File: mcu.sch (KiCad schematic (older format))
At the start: 44 parts, among them J10 DX07S016JA1R1500, J11 I2Sext_SD, J12 I2S_SD, J13 SDOUT, J14 ~CSB, J15 I2S2_MCK, J16 WCLK, J17 BCLK, J18 SCLK, J7 PD0-7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

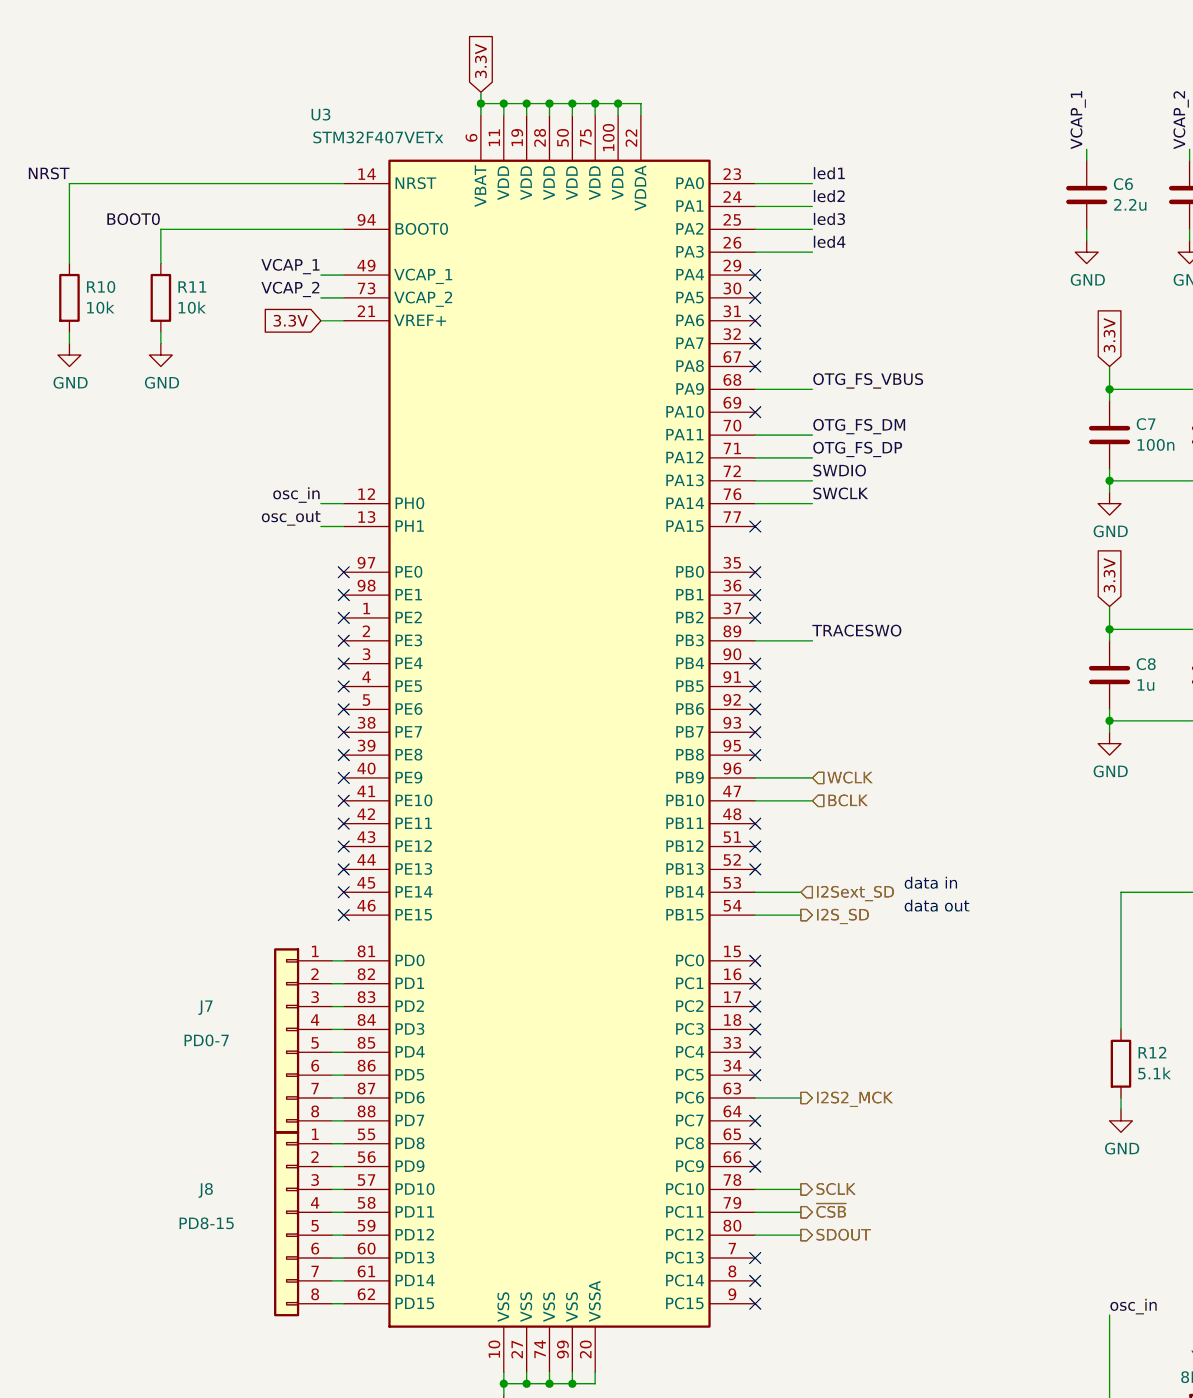
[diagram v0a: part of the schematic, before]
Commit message: Update pins for actual ADC ins
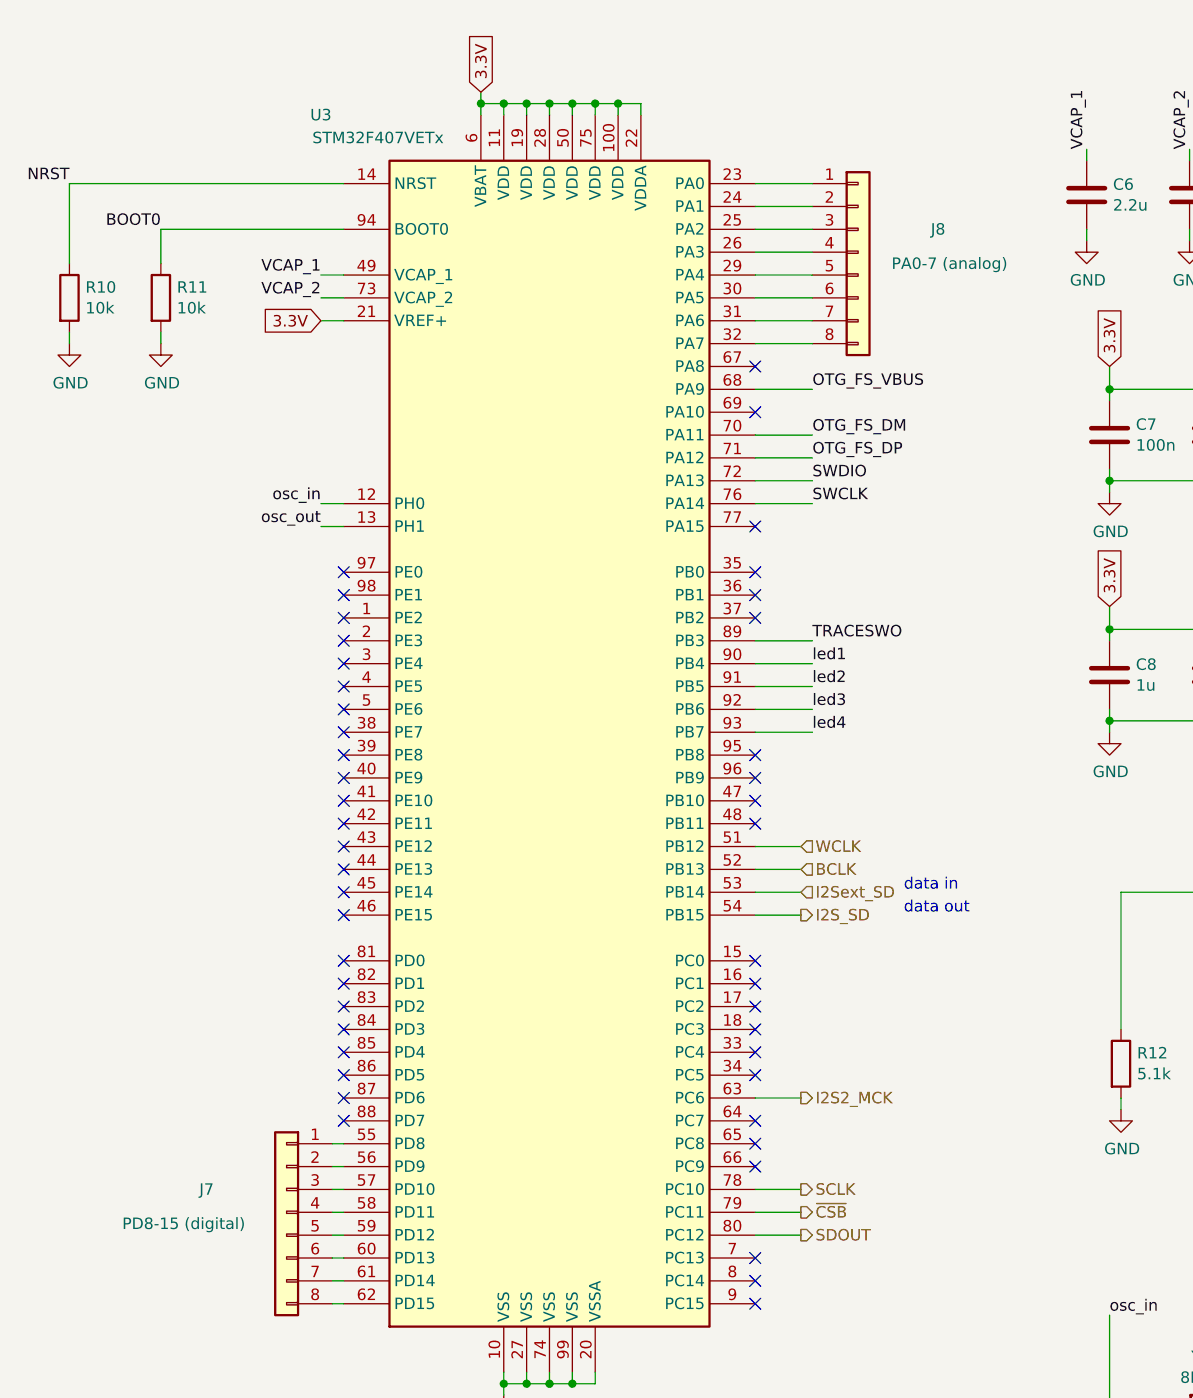
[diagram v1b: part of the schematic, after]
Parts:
- removed J7: PD0-7, Connector_PinHeader_2.54mm:PinHeader_1x08_P2.54mm_Vertical, symbol Connector_Generic:Conn_01x08
- added J8: PA0-7 (analog), Connector_PinHeader_2.54mm:PinHeader_1x08_P2.54mm_Vertical, symbol Connector_Generic:Conn_01x08
- J7: renamed from J8; value PD8-15 -> PD8-15 (digital)
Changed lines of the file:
@@
 	1950 5400 2000 5400
 $Comp
-L Connector_Generic:Conn_01x08 J8
+L Connector_Generic:Conn_01x08 J7
 U 1 1 605BF3D9
 P 1750 5700
-F 0 "J8" H 2100 5800 50  0000 C CNN
-F 1 "PD8-15" H 2100 5650 50  0000 C CNN
+F 0 "J7" H 2100 5800 50  0000 C CNN
+F 1 "PD8-15 (digital)" H 2200 5650 50  0000 C CNN
 F 2 "Connector_PinHeader_2.54mm:PinHeader_1x08_P2.54mm_Vertical" H 1750 5700 50  0001 C CNN
 F 3 "~" H 1750 5700 50  0001 C CNN
 	1    1750 5700
-	-1   0    0    -1
-$EndComp
-$Comp
-L Connector_Generic:Conn_01x08 J7
-U 1 1 605777EA
-P 1750 4900
-F 0 "J7" H 2100 5000 50  0000 C CNN
-F 1 "PD0-7" H 2100 4850 50  0000 C CNN
-F 2 "Connector_PinHeader_2.54mm:PinHeader_1x08_P2.54mm_Vertical" H 1750 4900 50  0001 C CNN
-F 3 "~" H 1750 4900 50  0001 C CNN
-	1    1750 4900
 	-1   0    0    -1
 $EndComp
@@
 Wire Wire Line
 	4050 1200 3800 1200
-Text Label 4050 1500 0    50   ~ 0
+Text Label 4050 3600 0    50   ~ 0
 led4
-Text Label 4050 1400 0    50   ~ 0
+Text Label 4050 3500 0    50   ~ 0
 led3
-Text Label 4050 1300 0    50   ~ 0
+Text Label 4050 3400 0    50   ~ 0
 led2
-Text Label 4050 1200 0    50   ~ 0
+Text Label 4050 3300 0    50   ~ 0
 led1
-Wire Wire Line
-	1950 5300 2000 5300
-Wire Wire Line
-	1950 5200 2000 5200
-Wire Wire Line
-	1950 5100 2000 5100
-Wire Wire Line
-	1950 5000 2000 5000
-Wire Wire Line
-	1950 4900 2000 4900
-Wire Wire Line
-	1950 4800 2000 4800
-Wire Wire Line
-	1950 4700 2000 4700
-Wire Wire Line
-	1950 4600 2000 4600
 Text Label 1900 2700 2    50   ~ 0
 osc_out
@@
 SWDIO
 Wire Wire Line
-	4050 3900 3800 3900
-Wire Wire Line
-	4050 3800 3800 3800
+	4000 4200 3800 4200
+Wire Wire Line
+	4000 4100 3800 4100
 Text Notes 4450 4400 0    50   ~ 0
 data out
@@
 Text HLabel 4000 4400 2    50   Output ~ 0
 I2S_SD
-Text HLabel 4050 3800 2    50   Input ~ 0
+Text HLabel 4000 4100 2    50   Input ~ 0
 WCLK
-Text HLabel 4050 3900 2    50   Input ~ 0
+Text HLabel 4000 4200 2    50   Input ~ 0
 BCLK
 $Comp
@@
 NoConn ~ 2000 4400
 NoConn ~ 3800 4000
-NoConn ~ 3800 4100
-NoConn ~ 3800 4200
-NoConn ~ 3800 3300
-NoConn ~ 3800 3400
-NoConn ~ 3800 3500
-NoConn ~ 3800 3600
 NoConn ~ 3800 3700
 NoConn ~ 3800 2900
@@
 NoConn ~ 3800 2200
 NoConn ~ 3800 2000
-NoConn ~ 3800 1900
-NoConn ~ 3800 1800
-NoConn ~ 3800 1700
-NoConn ~ 3800 1600
 NoConn ~ 3800 4600
 NoConn ~ 3800 4700
@@
 NoConn ~ 3800 4900
 NoConn ~ 3800 4800
+NoConn ~ 3800 3800
+NoConn ~ 3800 3900
+$Comp
+L Connector_Generic:Conn_01x08 J8
+U 1 1 60E25F3D
+P 4250 1500
+F 0 "J8" H 4600 1600 50  0000 C CNN
+F 1 "PA0-7 (analog)" H 4650 1450 50  0000 C CNN
+F 2 "Connector_PinHeader_2.54mm:PinHeader_1x08_P2.54mm_Vertical" H 4250 1500 50  0001 C CNN
+F 3 "~" H 4250 1500 50  0001 C CNN
+	1    4250 1500
+	1    0    0    -1
+$EndComp
+Wire Wire Line
+	3800 1600 4050 1600
+Wire Wire Line
+	3800 1700 4050 1700
+Wire Wire Line
+	3800 1800 4050 1800
+Wire Wire Line
+	3800 1900 4050 1900
+Wire Wire Line
+	4050 3300 3800 3300
+Wire Wire Line
+	3800 3400 4050 3400
+Wire Wire Line
+	4050 3500 3800 3500
+Wire Wire Line
+	3800 3600 4050 3600
+NoConn ~ 2000 4600
+NoConn ~ 2000 4700
+NoConn ~ 2000 4800
+NoConn ~ 2000 4900
+NoConn ~ 2000 5000
+NoConn ~ 2000 5100
+NoConn ~ 2000 5200
+NoConn ~ 2000 5300
 $EndSCHEMATC

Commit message: Basically done?
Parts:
- removed J11: I2Sext_SD, Connector_PinHeader_2.54mm:PinHeader_1x02_P2.54mm_Vertical, symbol Connector_Generic:Conn_01x02
- removed J12: I2S_SD, Connector_PinHeader_2.54mm:PinHeader_1x02_P2.54mm_Vertical, symbol Connector_Generic:Conn_01x02
- removed J13: SDOUT, Connector_PinHeader_2.54mm:PinHeader_1x02_P2.54mm_Vertical, symbol Connector_Generic:Conn_01x02
- removed J14: ~CSB, Connector_PinHeader_2.54mm:PinHeader_1x02_P2.54mm_Vertical, symbol Connector_Generic:Conn_01x02
- removed J15: I2S2_MCK, Connector_PinHeader_2.54mm:PinHeader_1x02_P2.54mm_Vertical, symbol Connector_Generic:Conn_01x02
- removed J16: WCLK, Connector_PinHeader_2.54mm:PinHeader_1x02_P2.54mm_Vertical, symbol Connector_Generic:Conn_01x02
- removed J17: BCLK, Connector_PinHeader_2.54mm:PinHeader_1x02_P2.54mm_Vertical, symbol Connector_Generic:Conn_01x02
- removed J18: SCLK, Connector_PinHeader_2.54mm:PinHeader_1x02_P2.54mm_Vertical, symbol Connector_Generic:Conn_01x02
- added J11: Conn_02x08_Odd_Even, Connector_PinHeader_2.54mm:PinHeader_2x08_P2.54mm_Vertical, symbol Connector_Generic:Conn_02x08_Odd_Even
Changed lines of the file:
@@
 	1    0    0    -1
 $EndComp
-Text HLabel 8950 700  0    50   Input ~ 0
+Text HLabel 9700 2200 0    50   Input ~ 0
 I2Sext_SD
-Wire Wire Line
-	8950 700  9050 700
-Text HLabel 8950 1200 0    50   Output ~ 0
+Text HLabel 9700 1900 0    50   Output ~ 0
 I2S_SD
-Wire Wire Line
-	8950 1200 9050 1200
-Text HLabel 10250 2100 0    50   Output ~ 0
+Text HLabel 9700 1700 0    50   Output ~ 0
 SCLK
-Text HLabel 8950 2100 0    50   Output ~ 0
+Text HLabel 9700 1500 0    50   Output ~ 0
 ~CSB
-Wire Wire Line
-	8950 2100 9050 2100
-Wire Wire Line
-	10250 2100 10350 2100
-Wire Wire Line
-	10250 700  10350 700
-Wire Wire Line
-	10250 1200 10350 1200
-Text HLabel 10250 1200 0    50   Input ~ 0
+Text HLabel 9700 2000 0    50   Input ~ 0
 WCLK
-Text HLabel 10250 1650 0    50   Input ~ 0
+Text HLabel 9700 2100 0    50   Input ~ 0
 BCLK
-Wire Wire Line
-	10250 1650 10350 1650
-Text HLabel 10250 700  0    50   Output ~ 0
+Text HLabel 9700 1800 0    50   Output ~ 0
 I2S2_MCK
 $Comp
@@
 	1    0    0    -1
 $EndComp
-$Comp
-L Connector_Generic:Conn_01x02 J11
-U 1 1 6077F6F7
-P 9250 700
-F 0 "J11" H 9330 692 50  0000 L CNN
-F 1 "I2Sext_SD" H 9330 601 50  0000 L CNN
-F 2 "Connector_PinHeader_2.54mm:PinHeader_1x02_P2.54mm_Vertical" H 9250 700 50  0001 C CNN
-F 3 "~" H 9250 700 50  0001 C CNN
-	1    9250 700
-	1    0    0    -1
-$EndComp
-$Comp
-L power:GND #PWR028
-U 1 1 60780EDB
-P 8950 800
-F 0 "#PWR028" H 8950 550 50  0001 C CNN
-F 1 "GND" H 8955 627 50  0000 C CNN
-F 2 "" H 8950 800 50  0001 C CNN
-F 3 "" H 8950 800 50  0001 C CNN
-	1    8950 800
-	1    0    0    -1
-$EndComp
-Wire Wire Line
-	8950 800  9050 800
-$Comp
-L Connector_Generic:Conn_01x02 J12
-U 1 1 607AA4FF
-P 9250 1200
-F 0 "J12" H 9330 1192 50  0000 L CNN
-F 1 "I2S_SD" H 9330 1101 50  0000 L CNN
-F 2 "Connector_PinHeader_2.54mm:PinHeader_1x02_P2.54mm_Vertical" H 9250 1200 50  0001 C CNN
-F 3 "~" H 9250 1200 50  0001 C CNN
-	1    9250 1200
-	1    0    0    -1
-$EndComp
-$Comp
-L power:GND #PWR029
-U 1 1 607AA505
-P 8950 1300
-F 0 "#PWR029" H 8950 1050 50  0001 C CNN
-F 1 "GND" H 8955 1127 50  0000 C CNN
-F 2 "" H 8950 1300 50  0001 C CNN
-F 3 "" H 8950 1300 50  0001 C CNN
-	1    8950 1300
-	1    0    0    -1
-$EndComp
-Wire Wire Line
-	8950 1300 9050 1300
-$Comp
-L Connector_Generic:Conn_01x02 J13
-U 1 1 607C35A1
-P 9250 1650
-F 0 "J13" H 9330 1642 50  0000 L CNN
-F 1 "SDOUT" H 9330 1551 50  0000 L CNN
-F 2 "Connector_PinHeader_2.54mm:PinHeader_1x02_P2.54mm_Vertical" H 9250 1650 50  0001 C CNN
-F 3 "~" H 9250 1650 50  0001 C CNN
-	1    9250 1650
-	1    0    0    -1
-$EndComp
-$Comp
-L power:GND #PWR030
-U 1 1 607C35A7
-P 8950 1750
-F 0 "#PWR030" H 8950 1500 50  0001 C CNN
-F 1 "GND" H 8955 1577 50  0000 C CNN
-F 2 "" H 8950 1750 50  0001 C CNN
-F 3 "" H 8950 1750 50  0001 C CNN
-	1    8950 1750
-	1    0    0    -1
-$EndComp
-Wire Wire Line
-	8950 1750 9050 1750
-Wire Wire Line
-	8950 1650 9050 1650
-Text HLabel 8950 1650 0    50   Output ~ 0
+Text HLabel 9700 1600 0    50   Output ~ 0
 SDOUT
-$Comp
-L Connector_Generic:Conn_01x02 J14
-U 1 1 60810229
-P 9250 2100
-F 0 "J14" H 9330 2098 50  0000 L CNN
-F 1 "~CSB" H 9330 2000 50  0000 L CNN
-F 2 "Connector_PinHeader_2.54mm:PinHeader_1x02_P2.54mm_Vertical" H 9250 2100 50  0001 C CNN
-F 3 "~" H 9250 2100 50  0001 C CNN
-	1    9250 2100
-	1    0    0    -1
-$EndComp
-$Comp
-L power:GND #PWR031
-U 1 1 6081022F
-P 8950 2200
-F 0 "#PWR031" H 8950 1950 50  0001 C CNN
-F 1 "GND" H 8955 2027 50  0000 C CNN
-F 2 "" H 8950 2200 50  0001 C CNN
-F 3 "" H 8950 2200 50  0001 C CNN
-	1    8950 2200
-	1    0    0    -1
-$EndComp
-Wire Wire Line
-	8950 2200 9050 2200
-$Comp
-L Connector_Generic:Conn_01x02 J18
-U 1 1 60829A8A
-P 10550 2100
-F 0 "J18" H 10630 2092 50  0000 L CNN
-F 1 "SCLK" H 10630 2001 50  0000 L CNN
-F 2 "Connector_PinHeader_2.54mm:PinHeader_1x02_P2.54mm_Vertical" H 10550 2100 50  0001 C CNN
-F 3 "~" H 10550 2100 50  0001 C CNN
-	1    10550 2100
-	1    0    0    -1
-$EndComp
-$Comp
-L power:GND #PWR035
-U 1 1 60829A90
-P 10250 2200
-F 0 "#PWR035" H 10250 1950 50  0001 C CNN
-F 1 "GND" H 10255 2027 50  0000 C CNN
-F 2 "" H 10250 2200 50  0001 C CNN
-F 3 "" H 10250 2200 50  0001 C CNN
-	1    10250 2200
-	1    0    0    -1
-$EndComp
-Wire Wire Line
-	10250 2200 10350 2200
-$Comp
-L Connector_Generic:Conn_01x02 J15
-U 1 1 60842B65
-P 10550 700
-F 0 "J15" H 10630 692 50  0000 L CNN
-F 1 "I2S2_MCK" H 10630 601 50  0000 L CNN
-F 2 "Connector_PinHeader_2.54mm:PinHeader_1x02_P2.54mm_Vertical" H 10550 700 50  0001 C CNN
-F 3 "~" H 10550 700 50  0001 C CNN
-	1    10550 700
-	1    0    0    -1
-$EndComp
-$Comp
-L power:GND #PWR032
-U 1 1 60842B6B
-P 10250 800
-F 0 "#PWR032" H 10250 550 50  0001 C CNN
-F 1 "GND" H 10255 627 50  0000 C CNN
-F 2 "" H 10250 800 50  0001 C CNN
-F 3 "" H 10250 800 50  0001 C CNN
-	1    10250 800
-	1    0    0    -1
-$EndComp
-Wire Wire Line
-	10250 800  10350 800
-$Comp
-L Connector_Generic:Conn_01x02 J16
-U 1 1 6085C09F
-P 10550 1200
-F 0 "J16" H 10630 1192 50  0000 L CNN
-F 1 "WCLK" H 10630 1101 50  0000 L CNN
-F 2 "Connector_PinHeader_2.54mm:PinHeader_1x02_P2.54mm_Vertical" H 10550 1200 50  0001 C CNN
-F 3 "~" H 10550 1200 50  0001 C CNN
-	1    10550 1200
-	1    0    0    -1
-$EndComp
-$Comp
-L power:GND #PWR033
-U 1 1 6085C0A5
-P 10250 1300
-F 0 "#PWR033" H 10250 1050 50  0001 C CNN
-F 1 "GND" H 10255 1127 50  0000 C CNN
-F 2 "" H 10250 1300 50  0001 C CNN
-F 3 "" H 10250 1300 50  0001 C CNN
-	1    10250 1300
-	1    0    0    -1
-$EndComp
-Wire Wire Line
-	10250 1300 10350 1300
-$Comp
-L Connector_Generic:Conn_01x02 J17
-U 1 1 60875BE1
-P 10550 1650
-F 0 "J17" H 10630 1642 50  0000 L CNN
-F 1 "BCLK" H 10630 1551 50  0000 L CNN
-F 2 "Connector_PinHeader_2.54mm:PinHeader_1x02_P2.54mm_Vertical" H 10550 1650 50  0001 C CNN
-F 3 "~" H 10550 1650 50  0001 C CNN
-	1    10550 1650
-	1    0    0    -1
-$EndComp
-$Comp
-L power:GND #PWR034
-U 1 1 60875BE7
-P 10250 1750
-F 0 "#PWR034" H 10250 1500 50  0001 C CNN
-F 1 "GND" H 10255 1577 50  0000 C CNN
-F 2 "" H 10250 1750 50  0001 C CNN
-F 3 "" H 10250 1750 50  0001 C CNN
-	1    10250 1750
-	1    0    0    -1
-$EndComp
-Wire Wire Line
-	10250 1750 10350 1750
 NoConn ~ 2000 2900
 NoConn ~ 2000 3000
@@
 NoConn ~ 2000 5200
 NoConn ~ 2000 5300
+Connection ~ 10300 1800
+$Comp
+L power:GND #PWR028
+U 1 1 604BFE47
+P 10550 1800
+F 0 "#PWR028" H 10550 1550 50  0001 C CNN
+F 1 "GND" H 10555 1627 50  0000 C CNN
+F 2 "" H 10550 1800 50  0001 C CNN
+F 3 "" H 10550 1800 50  0001 C CNN
+	1    10550 1800
+	1    0    0    -1
+$EndComp
+Wire Wire Line
+	10550 1800 10300 1800
+Wire Wire Line
+	9700 2200 9800 2200
+Wire Wire Line
+	9700 2100 9800 2100
+Wire Wire Line
+	9800 2000 9700 2000
+Wire Wire Line
+	9700 1900 9800 1900
+Wire Wire Line
+	9800 1800 9700 1800
+Wire Wire Line
+	9700 1700 9800 1700
+Wire Wire Line
+	9800 1600 9700 1600
+Wire Wire Line
+	9700 1500 9800 1500
+Wire Wire Line
+	10300 1800 10300 1900
+$Comp
+L Connector_Generic:Conn_02x08_Odd_Even J11
+U 1 1 605770D1
+P 10000 1800
+F 0 "J11" H 10050 2317 50  0000 C CNN
+F 1 "Conn_02x08_Odd_Even" H 10050 2226 50  0000 C CNN
+F 2 "Connector_PinHeader_2.54mm:PinHeader_2x08_P2.54mm_Vertical" H 10000 1800 50  0001 C CNN
+F 3 "~" H 10000 1800 50  0001 C CNN
+	1    10000 1800
+	1    0    0    -1
+$EndComp
+Wire Wire Line
+	10300 2100 10300 2200
+Wire Wire Line
+	10300 1700 10300 1800
+Wire Wire Line
+	10300 1900 10300 2000
+Connection ~ 10300 1900
+Wire Wire Line
+	10300 2000 10300 2100
+Connection ~ 10300 2000
+Connection ~ 10300 2100
+Wire Wire Line
+	10300 1500 10300 1600
+Wire Wire Line
+	10300 1600 10300 1700
+Connection ~ 10300 1600
+Connection ~ 10300 1700
 $EndSCHEMATC

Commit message: 4 layer progress
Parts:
- J10: symbol USB_C:DX07S016JA1R1500 -> dsp_dev_board-rescue:DX07S016JA1R1500-USB_C
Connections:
- wire segments 188 -> 190
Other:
- moved on the sheet: R10
